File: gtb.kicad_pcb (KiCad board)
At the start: 2 copper layers, 34.3 x 25.4 mm, 7 parts, among them U1 7555

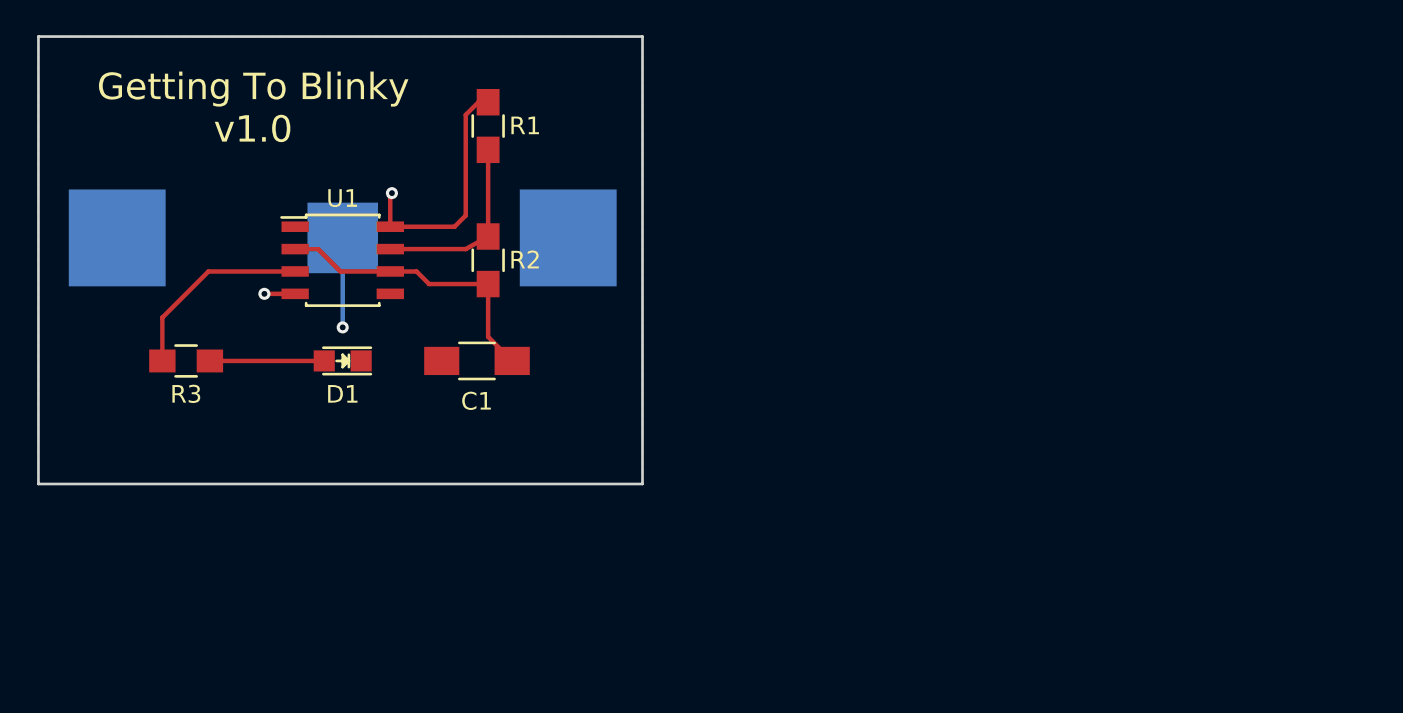
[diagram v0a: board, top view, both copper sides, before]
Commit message: updated with smaller board
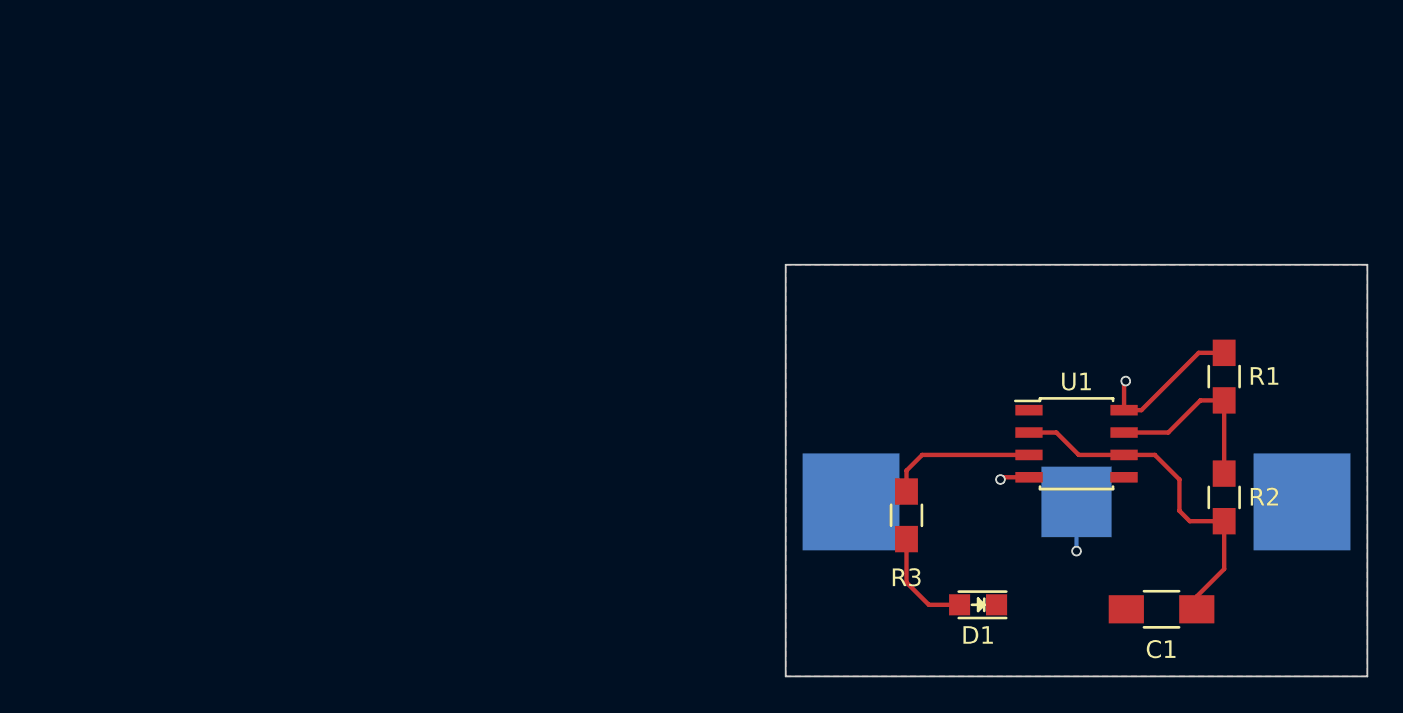
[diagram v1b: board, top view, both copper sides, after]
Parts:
- moved BT1 44.3 mm to (147.1, 106.4)
- moved R1 44.1 mm to (155.4, 99.3)
- moved R2 43.9 mm to (155.4, 106.2)
- moved U1 42.9 mm to (147.1, 103.1)
- moved R3 41.8 mm to (137.4, 107.2), turned to 270 degrees
- moved C1 41.3 mm to (151.9, 112.5)
- moved D1 38.6 mm to (141.5, 112.3)
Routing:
- net /VDD: track 15.5 -> 10.4 mm
- net Net-(C1-Pad1): track 16.7 -> 19.9 mm
- net Net-(R3-Pad1): track 11.1 -> 8.51 mm
- net GND: track 5.08 -> 2.79 mm
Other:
- board size 34.3 x 25.4 mm -> 33 x 23.4 mm
- net class Default: clearance 0.254 -> 0.2; trace_width 0.254 -> 0.25; via_dia 0.6858 -> 0.6; via_drill 0.3302 -> 0.4
- rule pad_to_mask_clearance: 0.2 -> 0
- rule trace_clearance: 0.254 -> 0.2
- rule trace_min: 0.1524 -> 0.2
- rule via_min_drill: 0.3302 -> 0.3
- rule via_min_size: 0.6858 -> 0.4
- board text removed: "Getting To Blinky v1.0"

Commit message: updated to remove Pin5 connection to ground and R3 to 100Ohm
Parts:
- R3: value 1K -> 100
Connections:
- U1 pad 5: GND -> Net-(U1-Pad5)
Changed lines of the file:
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@@
 (kicad_pcb (version 4) (host pcbnew 4.0.2-stable)
   (general
-    (links 15)
+    (links 14)
     (no_connects 0)
-    (area 130.505999 92.855 163.626001 117.561)
+    (area 130.505999 92.913999 163.626001 116.382001)
     (thickness 1.6)
     (drawings 4)
@@
     (zones 0)
     (modules 7)
-    (nets 7)
+    (nets 8)
   )
   (page A4)
   (layers
     (0 F.Cu signal)
-    (31 B.Cu signal)
+    (31 B.Cu signal hide)
     (32 B.Adhes user)
     (33 F.Adhes user)
@@
   (net 5 "Net-(R1-Pad2)")
   (net 6 "Net-(R3-Pad1)")
+  (net 7 "Net-(U1-Pad5)")
   (net_class Default "This is the default net class."
     (clearance 0.2)
@@
     (add_net "Net-(R1-Pad2)")
     (add_net "Net-(R3-Pad1)")
+    (add_net "Net-(U1-Pad5)")
   )
   (module gtb:S8211R (layer B.Cu)
@@
       (effects (font (size 1 1) (thickness 0.15)))
     )
-    (fp_text value 1K (at 0 2.1 270) (layer F.Fab)
+    (fp_text value 100 (at 0 2.1 270) (layer F.Fab)
       (effects (font (size 1 1) (thickness 0.15)))
     )
@@
       (net 2 /VDD))
     (pad 5 smd rect (at 2.7 1.905) (size 1.55 0.6) (layers F.Cu F.Paste F.Mask)
-      (net 1 GND))
+      (net 7 "Net-(U1-Pad5)"))
     (pad 6 smd rect (at 2.7 0.635) (size 1.55 0.6) (layers F.Cu F.Paste F.Mask)
       (net 3 "Net-(C1-Pad1)"))
